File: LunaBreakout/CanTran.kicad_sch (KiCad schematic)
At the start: 7 parts, among them U5 MCP25625x-x-ML, Y2 Crystal_GND24

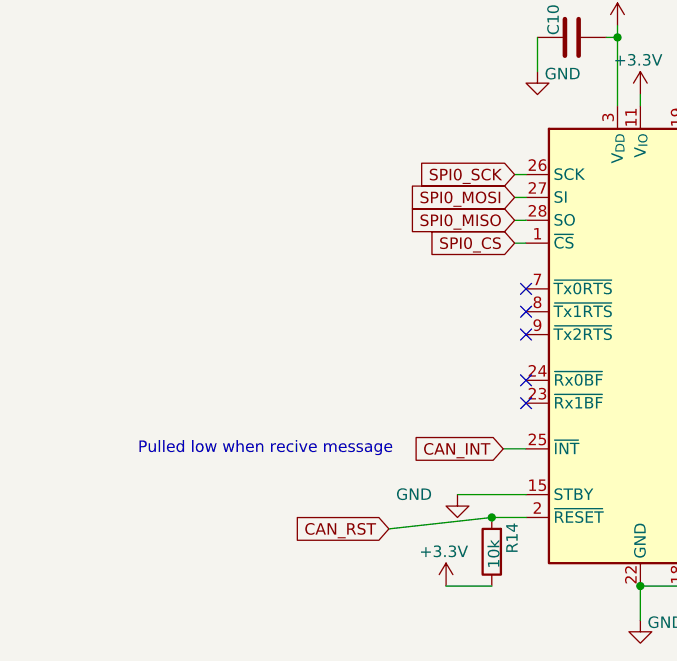
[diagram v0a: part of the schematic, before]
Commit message: Fixed net labels, added connectors for the communication ports added
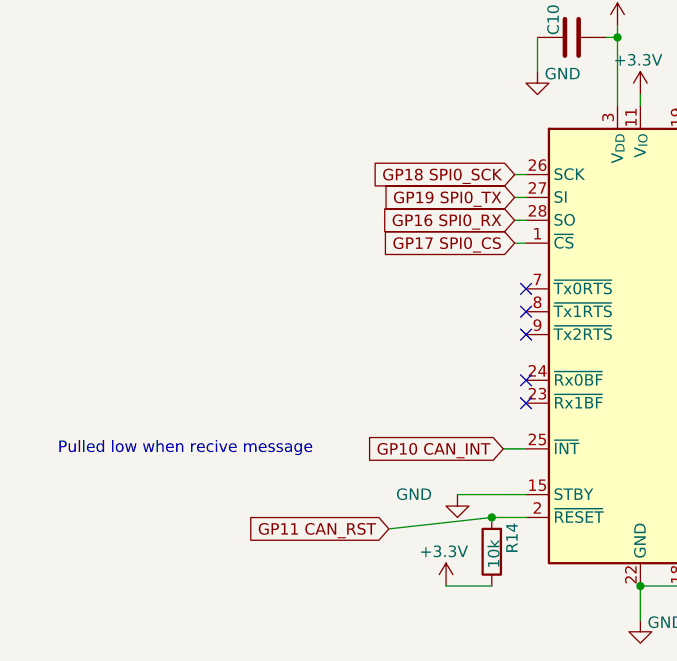
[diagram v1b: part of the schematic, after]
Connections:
- net CAN_INT renamed GP10 CAN_INT
- net CAN_RST renamed GP11 CAN_RST
- net SPI0_CS renamed GP17 SPI0_CS
- net SPI0_MISO renamed GP16 SPI0_RX
- net SPI0_MOSI renamed GP19 SPI0_TX
- net SPI0_SCK renamed GP18 SPI0_SCK
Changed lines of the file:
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@@
 	(text "Pulled low when recive message"
 		(exclude_from_sim no)
-		(at 166.624 80.01 0)
+		(at 157.734 80.01 0)
 		(effects
 			(font
@@
 		)
 	)
-	(global_label "SPI0_CS"
+	(global_label "GP17 SPI0_CS"
 		(shape input)
 		(at 194.31 57.15 180)
@@
 		)
 		(property "Intersheetrefs" "${INTERSHEET_REFS}"
-			(at 183.5839 57.15 0)
+			(at 177.6573 57.15 0)
 			(hide yes)
 			(show_name no)
@@
 		)
 	)
-	(global_label "CAN_INT"
+	(global_label "GP10 CAN_INT"
 		(shape input)
 		(at 193.04 80.01 180)
@@
 		)
 		(property "Intersheetrefs" "${INTERSHEET_REFS}"
-			(at 182.4952 80.01 0)
+			(at 176.5686 80.01 0)
 			(hide yes)
 			(show_name no)
@@
 		)
 	)
-	(global_label "SPI0_MOSI"
+	(global_label "GP19 SPI0_TX"
 		(shape input)
 		(at 194.31 52.07 180)
@@
 		)
 		(property "Intersheetrefs" "${INTERSHEET_REFS}"
-			(at 181.4672 52.07 0)
+			(at 177.9597 52.07 0)
 			(hide yes)
 			(show_name no)
@@
 		)
 	)
-	(global_label "SPI0_SCK"
+	(global_label "GP18 SPI0_SCK"
 		(shape input)
 		(at 194.31 49.53 180)
@@
 		)
 		(property "Intersheetrefs" "${INTERSHEET_REFS}"
-			(at 182.3139 49.53 0)
+			(at 176.3873 49.53 0)
 			(hide yes)
 			(show_name no)
@@
 		)
 	)
-	(global_label "SPI0_MISO"
+	(global_label "GP16 SPI0_RX"
 		(shape input)
 		(at 194.31 54.61 180)
@@
 		)
 		(property "Intersheetrefs" "${INTERSHEET_REFS}"
-			(at 181.4672 54.61 0)
+			(at 177.6573 54.61 0)
 			(hide yes)
 			(show_name no)
@@
 		)
 	)
-	(global_label "CAN_RST"
+	(global_label "GP11 CAN_RST"
 		(shape input)
 		(at 180.34 88.9 180)
@@
 		)
 		(property "Intersheetrefs" "${INTERSHEET_REFS}"
-			(at 169.251 88.9 0)
-			(hide yes)
-			(show_name no)
+			(at 163.3244 88.9 0)
+			(hide yes)
+			(show_name no)

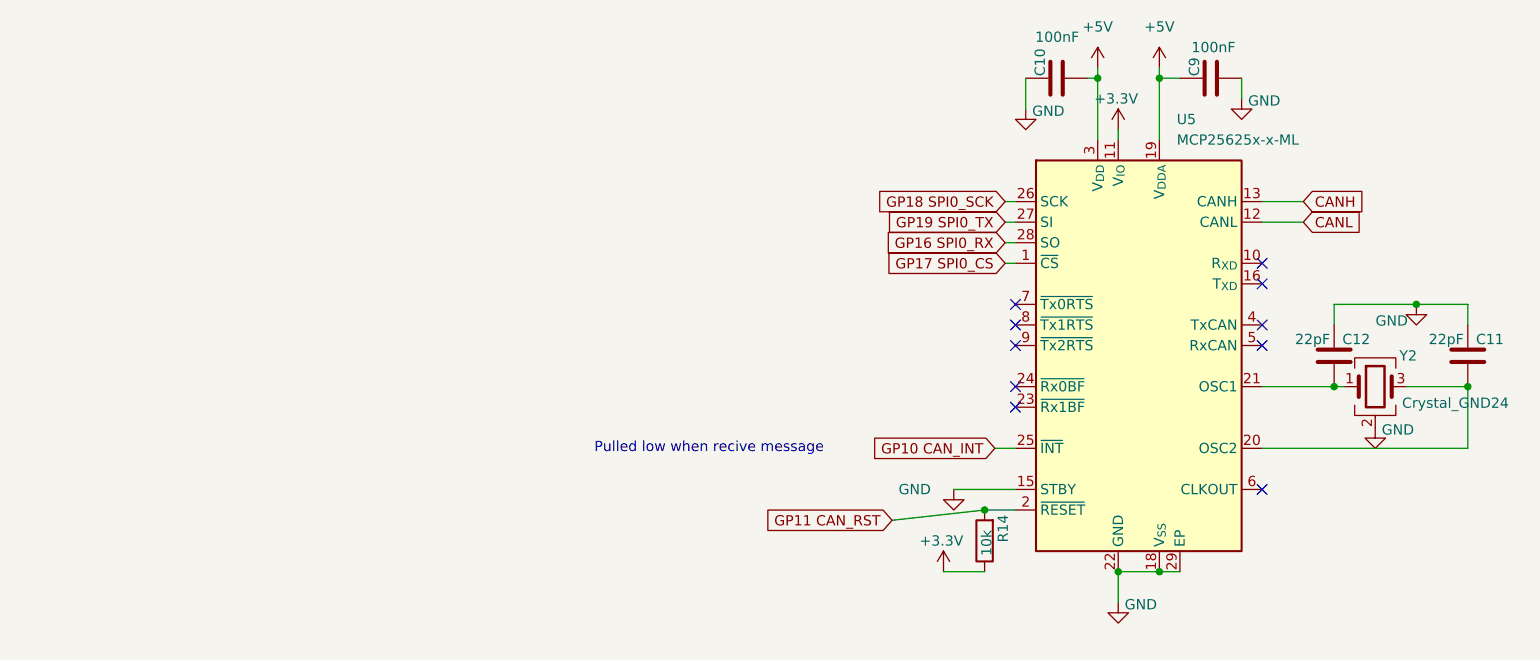
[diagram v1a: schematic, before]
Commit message: Took CAN out of schematic, changes connectorst, added misc connectors and external power symbol
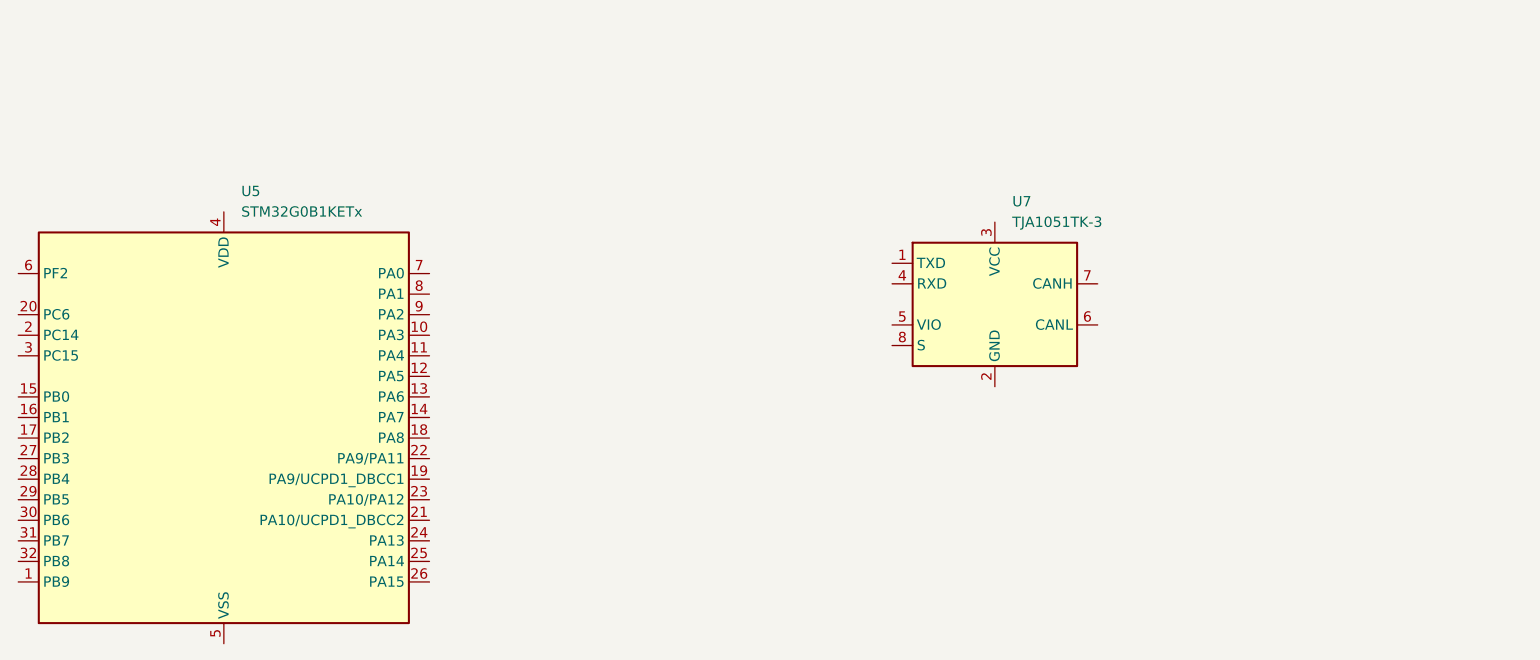
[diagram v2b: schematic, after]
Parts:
- removed C10, C9: 100nF, Capacitor_SMD:C_0805_2012Metric, symbol Device:C
- removed C11, C12: 22pF, Capacitor_SMD:C_0805_2012Metric, symbol Device:C
- removed R14: 10k, Resistor_SMD:R_0805_2012Metric, symbol Device:R
- removed U5: MCP25625x-x-ML, Package_DFN_QFN:QFN-28-1EP_6x6mm_P0.65mm_EP4.25x4.25mm, symbol Interface_CAN_LIN:MCP25625x-x-ML
- removed Y2: Crystal_GND24, Crystal:Crystal_SMD_Abracon_ABM8G-4Pin_3.2x2.5mm, symbol Device:Crystal_GND24
- added U5: STM32G0B1KETx, Package_QFP:LQFP-32_7x7mm_P0.8mm, symbol MCU_ST_STM32G0:STM32G0B1KETx
- added U7: TJA1051TK-3, Package_SON:HVSON-8-1EP_3x3mm_P0.65mm_EP1.6x2.4mm, symbol Interface_CAN_LIN:TJA1051TK-3
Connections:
- new net: U7.2 (GND), U7.9 (GND)
- no-connect marks 10 -> 0
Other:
- note removed: "Pulled low when recive message"
